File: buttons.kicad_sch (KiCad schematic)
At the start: 16 parts, among them J1 Conn_01x02, SW1 SW_SPST, SW2 SW_SPST, U1 TLC555xP, U2 74LS14

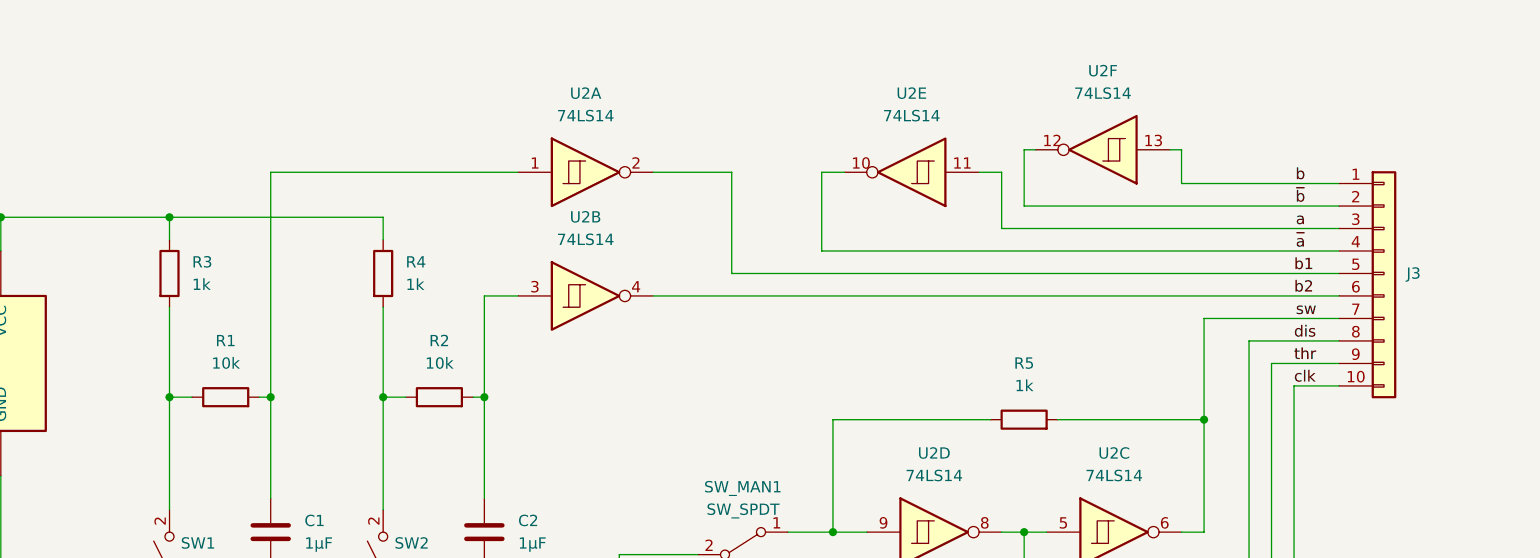
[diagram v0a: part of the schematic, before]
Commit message: simplified pcb layout
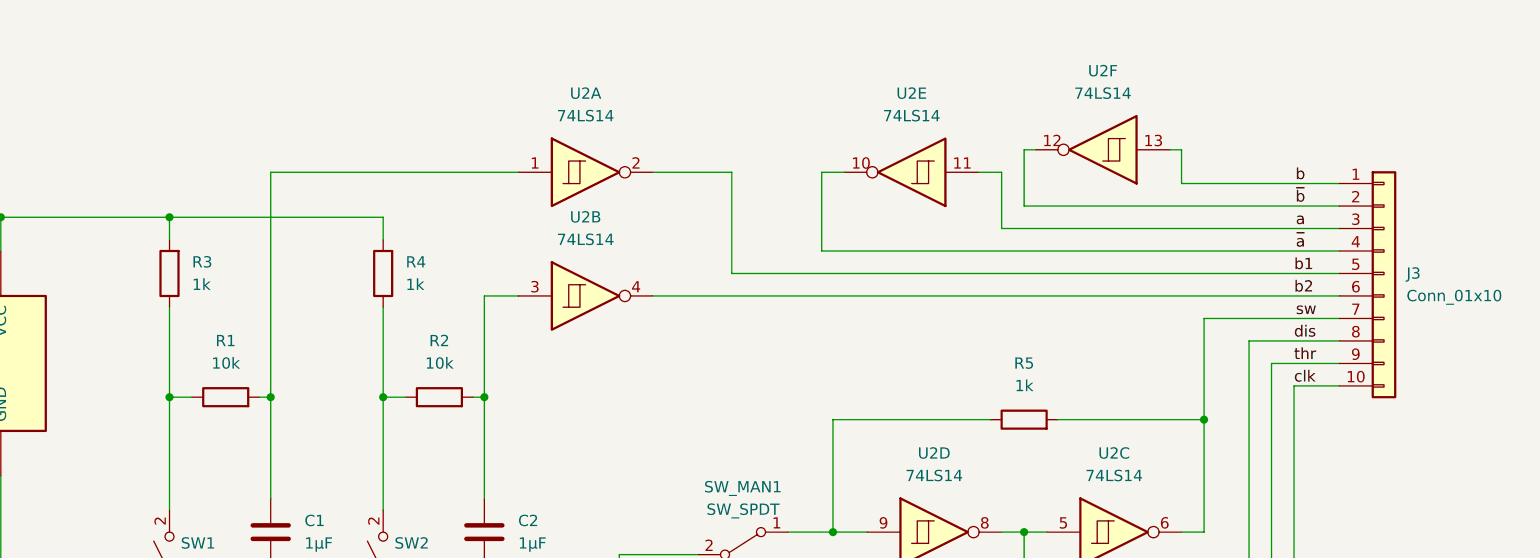
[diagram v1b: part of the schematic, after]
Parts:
- J3: value (none) -> Conn_01x10; footprint (none) -> Connector_PinHeader_2.54mm:PinHeader_1x10_P2.54mm_Vertical
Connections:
- net VCC: now also R3.2, R4.2; no longer R3.1, R4.1
- net at R2.1, SW2.2 (B): now also R4.1; no longer R4.2
- net at R1.1, SW1.2 (B): now also R3.1; no longer R3.2
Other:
- moved on the sheet: R3, R4
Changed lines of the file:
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@@
     (pin "7")
   )
-  (symbol (lib_id "Device:R") (at 130.81 63.5 0) (unit 1)
+  (symbol (lib_id "Device:R") (at 130.81 63.5 180) (unit 1)
     (in_bom yes) (on_board yes) (fields_autoplaced)
     (property "Reference" "R3" (id 0) (at 133.35 62.2299 0)
-      (effects (font (size 1.27 1.27)) (justify left))
+      (effects (font (size 1.27 1.27)) (justify right))
     )
     (property "Value" "1k" (id 1) (at 133.35 64.7699 0)
-      (effects (font (size 1.27 1.27)) (justify left))
-    )
-    (property "Footprint" "Resistor_THT:R_Axial_DIN0207_L6.3mm_D2.5mm_P2.54mm_Vertical" (id 2) (at 129.032 63.5 90)
+      (effects (font (size 1.27 1.27)) (justify right))
+    )
+    (property "Footprint" "Resistor_THT:R_Axial_DIN0207_L6.3mm_D2.5mm_P2.54mm_Vertical" (id 2) (at 132.588 63.5 90)
       (effects (font (size 1.27 1.27)) hide)
     )
@@
       (effects (font (size 1.27 1.27)) (justify left))
     )
-    (property "Value" "" (id 1) (at 270.51 66.0399 0)
-      (effects (font (size 1.27 1.27)) (justify left))
-    )
-    (property "Footprint" "" (id 2) (at 267.97 63.5 0)
+    (property "Value" "Conn_01x10" (id 1) (at 270.51 66.0399 0)
+      (effects (font (size 1.27 1.27)) (justify left))
+    )
+    (property "Footprint" "Connector_PinHeader_2.54mm:PinHeader_1x10_P2.54mm_Vertical" (id 2) (at 267.97 63.5 0)
       (effects (font (size 1.27 1.27)) hide)
     )
@@
     (pin "2")
   )
-  (symbol (lib_id "Device:R") (at 154.94 63.5 0) (unit 1)
+  (symbol (lib_id "Device:R") (at 154.94 63.5 180) (unit 1)
     (in_bom yes) (on_board yes) (fields_autoplaced)
     (property "Reference" "R4" (id 0) (at 157.48 62.2299 0)
-      (effects (font (size 1.27 1.27)) (justify left))
+      (effects (font (size 1.27 1.27)) (justify right))
     )
     (property "Value" "1k" (id 1) (at 157.48 64.7699 0)
-      (effects (font (size 1.27 1.27)) (justify left))
-    )
-    (property "Footprint" "Resistor_THT:R_Axial_DIN0207_L6.3mm_D2.5mm_P2.54mm_Vertical" (id 2) (at 153.162 63.5 90)
-      (effects (font (size 1.27 1.27)) hide)
-    )
+      (effects (font (size 1.27 1.27)) (justify right))
+    )
+    (property "Footprint" "Resistor_THT:R_Axial_DIN0207_L6.3mm_D2.5mm_P2.54mm_Vertical" (id 2) (at 156.718 63.5 90)
+      (effects (font (size 1.27 1.27)) hide)
+    )

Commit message: smaller refinements
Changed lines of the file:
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@@
   (junction (at 130.81 57.15) (diameter 0) (color 0 0 0 0)
   )
-  (junction (at 49.53 57.15) (diameter 0) (color 0 0 0 0)
-  )
   (junction (at 227.33 92.71) (diameter 0) (color 0 0 0 0)
   )
@@
   (junction (at 142.24 77.47) (diameter 0) (color 0 0 0 0)
   )
+  (junction (at 50.8 57.15) (diameter 0) (color 0 0 0 0)
+  )
   (junction (at 111.76 105.41) (diameter 0) (color 0 0 0 0)
   )
@@
     (stroke (width 0) (type default) (color 0 0 0 0))
   )
+  (wire (pts (xy 43.18 57.15) (xy 50.8 57.15))
+    (stroke (width 0) (type default) (color 0 0 0 0))
+  )
   (wire (pts (xy 166.37 66.04) (xy 170.18 66.04))
     (stroke (width 0) (type default) (color 0 0 0 0))
@@
     (stroke (width 0) (type default) (color 0 0 0 0))
   )
-  (wire (pts (xy 43.18 57.15) (xy 49.53 57.15))
-    (stroke (width 0) (type default) (color 0 0 0 0))
-  )
   (wire (pts (xy 227.33 49.53) (xy 227.33 55.88))
     (stroke (width 0) (type default) (color 0 0 0 0))
@@
     (stroke (width 0) (type default) (color 0 0 0 0))
   )
-  (wire (pts (xy 57.15 87.63) (xy 49.53 87.63))
+  (wire (pts (xy 57.15 87.63) (xy 50.8 87.63))
     (stroke (width 0) (type default) (color 0 0 0 0))
   )
@@
     (stroke (width 0) (type default) (color 0 0 0 0))
   )
-  (wire (pts (xy 49.53 57.15) (xy 69.85 57.15))
-    (stroke (width 0) (type default) (color 0 0 0 0))
-  )
   (wire (pts (xy 83.82 95.25) (xy 83.82 114.3))
     (stroke (width 0) (type default) (color 0 0 0 0))
@@
     (stroke (width 0) (type default) (color 0 0 0 0))
   )
+  (wire (pts (xy 50.8 57.15) (xy 69.85 57.15))
+    (stroke (width 0) (type default) (color 0 0 0 0))
+  )
   (wire (pts (xy 46.99 82.55) (xy 57.15 82.55))
     (stroke (width 0) (type default) (color 0 0 0 0))
@@
     (stroke (width 0) (type default) (color 0 0 0 0))
   )
-  (wire (pts (xy 49.53 87.63) (xy 49.53 57.15))
+  (wire (pts (xy 50.8 87.63) (xy 50.8 57.15))
     (stroke (width 0) (type default) (color 0 0 0 0))
   )
@@
     (pin "2")
   )
-  (symbol (lib_id "power:PWR_FLAG") (at 49.53 57.15 0) (unit 1)
+  (symbol (lib_id "power:PWR_FLAG") (at 50.8 57.15 0) (unit 1)
     (in_bom yes) (on_board yes) (fields_autoplaced)
-    (property "Reference" "#FLG01" (id 0) (at 49.53 55.245 0)
-      (effects (font (size 1.27 1.27)) hide)
-    )
-    (property "Value" "PWR_FLAG" (id 1) (at 49.53 52.07 0))
-    (property "Footprint" "" (id 2) (at 49.53 57.15 0)
-      (effects (font (size 1.27 1.27)) hide)
-    )
-    (property "Datasheet" "~" (id 3) (at 49.53 57.15 0)
-      (effects (font (size 1.27 1.27)) hide)
-    )
+    (property "Reference" "#FLG01" (id 0) (at 50.8 55.245 0)
+      (effects (font (size 1.27 1.27)) hide)
+    )
+    (property "Value" "PWR_FLAG" (id 1) (at 50.8 52.07 0))
+    (property "Footprint" "" (id 2) (at 50.8 57.15 0)
+      (effects (font (size 1.27 1.27)) hide)
+    )
+    (property "Datasheet" "~" (id 3) (at 50.8 57.15 0)
+      (effects (font (size 1.27 1.27)) hide)
+    )

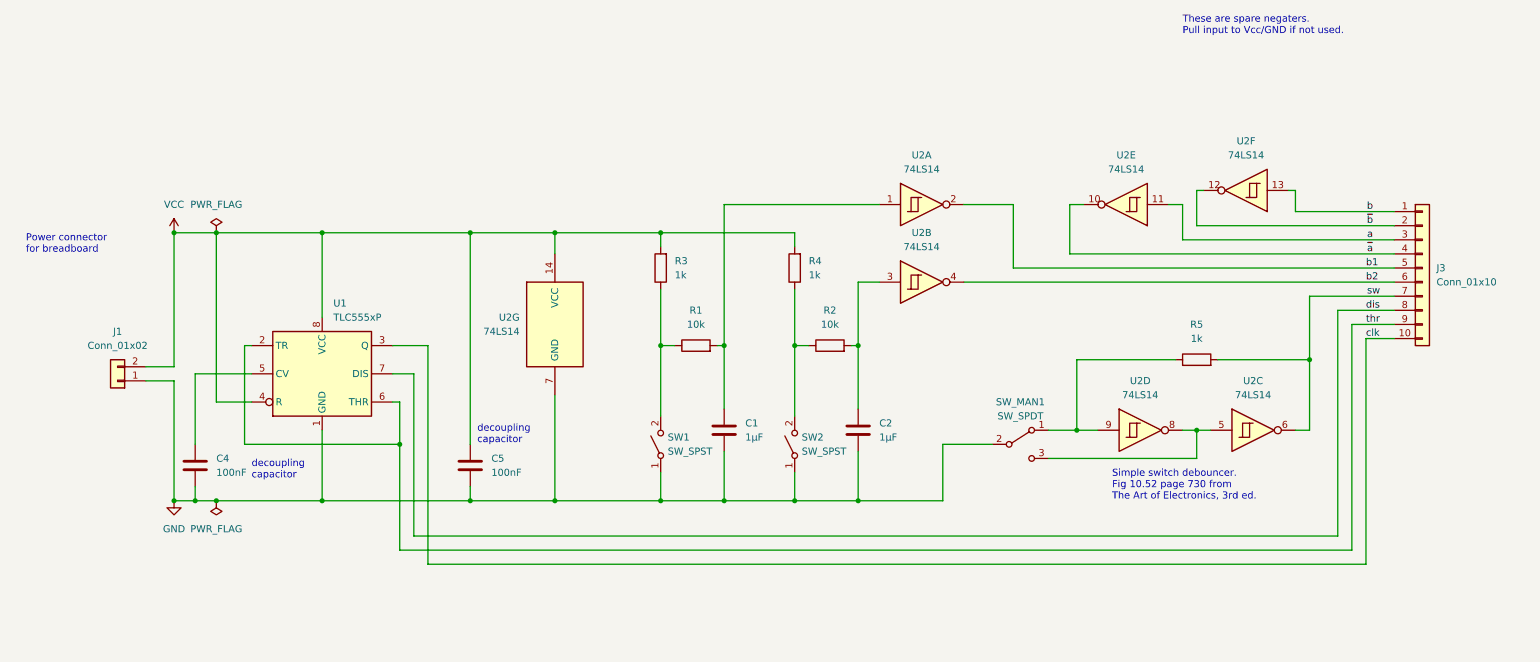
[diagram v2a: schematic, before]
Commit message: changed SPDT switch to standard jumper rail.
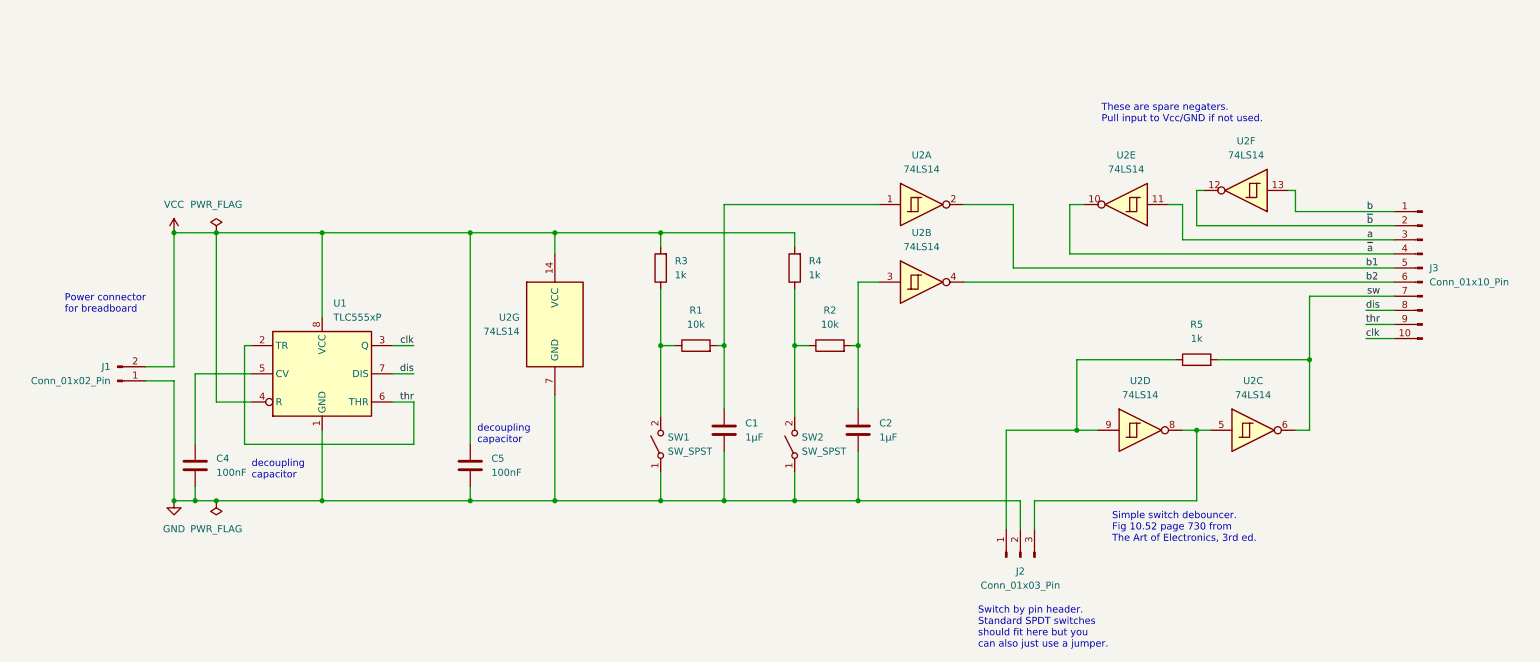
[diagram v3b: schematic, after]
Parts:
- removed J1: Conn_01x02, Connector_PinHeader_2.54mm:PinHeader_1x02_P2.54mm_Vertical, symbol Connector_Generic:Conn_01x02
- removed J3: Conn_01x10, Connector_PinHeader_2.54mm:PinHeader_1x10_P2.54mm_Vertical, symbol Connector_Generic:Conn_01x10
- removed SW_MAN1: SW_SPDT, Button_Switch_THT:Apem 25000N series, symbol Switch:SW_SPDT
- added J1: Conn_01x02_Pin, Connector_PinHeader_2.54mm:PinHeader_1x02_P2.54mm_Vertical, symbol Connector:Conn_01x02_Pin
- added J2: Conn_01x03_Pin, Connector_PinHeader_2.54mm:PinHeader_1x03_P2.54mm_Vertical, symbol Connector:Conn_01x03_Pin
- added J3: Conn_01x10_Pin, Connector_PinHeader_2.54mm:PinHeader_1x10_P2.54mm_Vertical, symbol Connector:Conn_01x10_Pin
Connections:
- net GND: now also J1.1 (Pin_1), J2.2 (Pin_2)
- net VCC: now also J1.2 (Pin_2)
- net a: now also J3.3 (Pin_3)
- net b: now also J3.1 (Pin_1)
- net b1: now also J3.5 (Pin_5)
- net b2: now also J3.6 (Pin_6)
- net clk: now also J3.10 (Pin_10)
- net dis: now also J3.8 (Pin_8)
- net sw: now also J3.7 (Pin_7)
- net thr: now also J3.9 (Pin_9)
- net ~{a}: now also J3.4 (Pin_4)
- net ~{b}: now also J3.2 (Pin_2)
- net at U2.5, U2.8: now also J2.3 (Pin_3)
- net at R5.1, U2.9: now also J2.1 (Pin_1)
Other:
- note added: "Switch by pin header. Standard SPDT switches should fit here but you can also just use a jumper."
